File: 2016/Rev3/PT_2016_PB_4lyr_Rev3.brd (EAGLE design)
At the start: 155.7 x 202.7 mm, 168 parts, among them Q1 MOSFET-NCHANNELFDD8780, Q12 2N7002, Q2 MMBT2222A, Q3 MOSFET-NCHANNELFDD8780, Q4 MMBT2222A

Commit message: Final Power Board 2016 Rev 2
generated gerbers
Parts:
- moved C4 0.25 mm to (63.5, 78.7)
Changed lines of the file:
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@@
 <setting verticaltext="up"/>
 </settings>
-<grid distance="0.005" unitdist="inch" unit="inch" style="lines" multiple="1" display="yes" altdistance="0.005" altunitdist="inch" altunit="inch"/>
+<grid distance="0.01" unitdist="inch" unit="inch" style="lines" multiple="1" display="yes" altdistance="0.005" altunitdist="inch" altunit="inch"/>
 <layers>
 <layer number="1" name="Top" color="4" fill="1" visible="yes" active="yes"/>
@@
 <layer number="17" name="Pads" color="11" fill="1" visible="yes" active="yes"/>
 <layer number="18" name="Vias" color="11" fill="1" visible="yes" active="yes"/>
-<layer number="19" name="Unrouted" color="6" fill="1" visible="yes" active="yes"/>
+<layer number="19" name="Unrouted" color="6" fill="1" visible="no" active="yes"/>
 <layer number="20" name="Dimension" color="13" fill="1" visible="yes" active="yes"/>
 <layer number="21" name="tPlace" color="7" fill="1" visible="yes" active="yes"/>
-<layer number="22" name="bPlace" color="7" fill="1" visible="yes" active="yes"/>
-<layer number="23" name="tOrigins" color="15" fill="1" visible="yes" active="yes"/>
-<layer number="24" name="bOrigins" color="15" fill="1" visible="yes" active="yes"/>
+<layer number="22" name="bPlace" color="7" fill="1" visible="no" active="yes"/>
+<layer number="23" name="tOrigins" color="15" fill="1" visible="no" active="yes"/>
+<layer number="24" name="bOrigins" color="15" fill="1" visible="no" active="yes"/>
 <layer number="25" name="tNames" color="7" fill="1" visible="no" active="yes"/>
 <layer number="26" name="bNames" color="7" fill="1" visible="no" active="yes"/>
@@
 <layer number="37" name="tTest" color="7" fill="1" visible="no" active="yes"/>
 <layer number="38" name="bTest" color="7" fill="1" visible="no" active="yes"/>
-<layer number="39" name="tKeepout" color="4" fill="11" visible="yes" active="yes"/>
+<layer number="39" name="tKeepout" color="4" fill="11" visible="no" active="yes"/>
 <layer number="40" name="bKeepout" color="1" fill="11" visible="no" active="yes"/>
-<layer number="41" name="tRestrict" color="4" fill="10" visible="yes" active="yes"/>
-<layer number="42" name="bRestrict" color="1" fill="10" visible="yes" active="yes"/>
+<layer number="41" name="tRestrict" color="4" fill="10" visible="no" active="yes"/>
+<layer number="42" name="bRestrict" color="1" fill="10" visible="no" active="yes"/>
 <layer number="43" name="vRestrict" color="2" fill="10" visible="no" active="yes"/>
 <layer number="44" name="Drills" color="7" fill="1" visible="no" active="yes"/>
-<layer number="45" name="Holes" color="7" fill="1" visible="no" active="yes"/>
+<layer number="45" name="Holes" color="7" fill="1" visible="yes" active="yes"/>
 <layer number="46" name="Milling" color="3" fill="1" visible="no" active="yes"/>
 <layer number="47" name="Measures" color="7" fill="1" visible="no" active="yes"/>
@@
 <layer number="49" name="Reference" color="7" fill="1" visible="yes" active="yes"/>
 <layer number="50" name="dxf" color="7" fill="1" visible="no" active="yes"/>
-<layer number="51" name="tDocu" color="7" fill="1" visible="yes" active="yes"/>
-<layer number="52" name="bDocu" color="7" fill="1" visible="yes" active="yes"/>
+<layer number="51" name="tDocu" color="7" fill="1" visible="no" active="yes"/>
+<layer number="52" name="bDocu" color="7" fill="1" visible="no" active="yes"/>
 <layer number="91" name="Nets" color="2" fill="1" visible="no" active="no"/>
 <layer number="92" name="Busses" color="1" fill="1" visible="no" active="no"/>
@@
 <text x="25.4" y="162.814" size="1.778" layer="21" font="vector" ratio="15" rot="SR270">+5V</text>
 <text x="25.4" y="148.59" size="1.778" layer="21" font="vector" ratio="15" rot="SR270">+12V</text>
-<text x="49.276" y="13.97" size="2.54" layer="21" ratio="15" rot="SR270">M1</text>
-<text x="49.53" y="29.718" size="2.54" layer="21" ratio="15" rot="SR270">M2</text>
-<text x="49.276" y="45.212" size="2.54" layer="21" ratio="15" rot="SR270">M3</text>
-<text x="49.276" y="61.214" size="2.54" layer="21" ratio="15" rot="SR270">M4</text>
-<text x="49.276" y="76.962" size="2.54" layer="21" ratio="15" rot="SR270">M5</text>
-<text x="49.276" y="92.456" size="2.54" layer="21" ratio="15" rot="SR270">M6</text>
-<text x="49.276" y="108.458" size="2.54" layer="21" ratio="15" rot="SR270">A1</text>
-<text x="49.276" y="124.206" size="2.54" layer="21" ratio="15" rot="SR270">A2</text>
-<text x="135.636" y="104.013" size="2.54" layer="21" font="vector" ratio="15" rot="R270">RS-485</text>
+<text x="49.276" y="13.97" size="2.54" layer="21" font="vector" ratio="15" rot="SR270">M1</text>
+<text x="49.53" y="29.718" size="2.54" layer="21" font="vector" ratio="15" rot="SR270">M2</text>
+<text x="49.276" y="45.212" size="2.54" layer="21" font="vector" ratio="15" rot="SR270">M3</text>
+<text x="49.276" y="61.214" size="2.54" layer="21" font="vector" ratio="15" rot="SR270">M4</text>
+<text x="49.276" y="76.962" size="2.54" layer="21" font="vector" ratio="15" rot="SR270">M5</text>
+<text x="49.276" y="92.456" size="2.54" layer="21" font="vector" ratio="15" rot="SR270">M6</text>
+<text x="49.276" y="108.458" size="2.54" layer="21" font="vector" ratio="15" rot="SR270">A1</text>
+<text x="49.276" y="124.206" size="2.54" layer="21" font="vector" ratio="15" rot="SR270">A2</text>
+<text x="135.636" y="104.013" size="2.54" layer="21" font="vector" ratio="10" rot="R270">RS-485</text>
 <text x="141.097" y="26.162" size="2.54" layer="21" font="vector" ratio="15" rot="SR270">+ -</text>
 <hole x="112.014" y="196.596" drill="3.199890625"/>
@@
 <param name="mtCopper" value="0.035559375mm 0.035559375mm 0.035559375mm 0.035559375mm 0.035559375mm 0.035559375mm 0.035559375mm 0.035559375mm 0.035559375mm 0.035559375mm 0.035559375mm 0.035559375mm 0.035559375mm 0.035559375mm 0.035559375mm 0.035559375mm"/>
 <param name="mtIsolate" value="1.501140625mm 0.149859375mm 0.200659375mm 0.149859375mm 0.200659375mm 0.149859375mm 0.200659375mm 0.149859375mm 0.200659375mm 0.149859375mm 0.200659375mm 0.149859375mm 0.200659375mm 0.149859375mm 0.200659375mm"/>
-<param name="mdWireWire" value="8mil"/>
-<param name="mdWirePad" value="8mil"/>
-<param name="mdWireVia" value="8mil"/>
-<param name="mdPadPad" value="8mil"/>
-<param name="mdPadVia" value="8mil"/>
-<param name="mdViaVia" value="8mil"/>
-<param name="mdSmdPad" value="8mil"/>
-<param name="mdSmdVia" value="8mil"/>
-<param name="mdSmdSmd" value="8mil"/>
+<param name="mdWireWire" value="5mil"/>
+<param name="mdWirePad" value="5mil"/>
+<param name="mdWireVia" value="5mil"/>
+<param name="mdPadPad" value="5mil"/>
+<param name="mdPadVia" value="5mil"/>
+<param name="mdViaVia" value="5mil"/>
+<param name="mdSmdPad" value="5mil"/>
+<param name="mdSmdVia" value="5mil"/>
+<param name="mdSmdSmd" value="5mil"/>
 <param name="mdViaViaSameLayer" value="8mil"/>
 <param name="mnLayersViaInSmd" value="2"/>
@@
 <element name="C2" library="MRDT-2014-All" package="C_12.5MM" value="1mF" x="63.5" y="51.308"/>
 <element name="C3" library="MRDT-2014-All" package="C_12.5MM" value="1mF" x="63.5" y="37.592"/>
-<element name="C4" library="MRDT-2014-All" package="C_12.5MM" value="1mF" x="63.5" y="78.486"/>
+<element name="C4" library="MRDT-2014-All" package="C_12.5MM" value="1mF" x="63.5" y="78.74"/>
 <element name="R3" library="resistor" package="R1206" value="100k 1%" x="85.598" y="136.652" rot="R270"/>
 <element name="R4" library="resistor" package="R1206" value="10kΩ 1%" x="88.138" y="136.652" rot="R90"/>
@@
 <wire x1="132.458" y1="146.05" x2="130.556" y2="146.05" width="0.3048" layer="1"/>
 <via x="130.556" y="146.05" extent="1-16" drill="0.381"/>
-<wire x1="130.556" y1="146.05" x2="115.697" y2="131.191" width="0.3048" layer="16"/>
-<wire x1="115.697" y1="131.191" x2="99.822" y2="131.191" width="0.3048" layer="16"/>
+<wire x1="130.556" y1="146.05" x2="115.697" y2="131.191" width="0.3048" layer="2"/>
+<wire x1="115.697" y1="131.191" x2="99.822" y2="131.191" width="0.3048" layer="2"/>
 </signal>
 <signal name="N$4">
@@
 <wire x1="153.519" y1="17.689" x2="146.431" y2="24.777" width="0.3048" layer="1"/>
 <wire x1="146.431" y1="24.777" x2="154.432" y2="32.778" width="0.762" layer="2"/>
-<wire x1="154.432" y1="32.778" x2="154.432" y2="188.214" width="0.762" layer="2"/>
-<wire x1="154.432" y1="188.214" x2="154.432" y2="194.818" width="0.762" layer="2"/>
+<wire x1="154.432" y1="32.778" x2="154.432" y2="188.976" width="0.762" layer="2"/>
+<wire x1="154.432" y1="188.976" x2="154.432" y2="194.818" width="0.762" layer="2"/>
 <wire x1="154.432" y1="194.818" x2="152.654" y2="196.596" width="0.762" layer="2"/>
-<wire x1="89.154" y1="196.596" x2="97.536" y2="188.214" width="0.762" layer="2"/>
-<wire x1="97.536" y1="188.214" x2="154.432" y2="188.214" width="0.762" layer="2"/>
-<wire x1="97.536" y1="188.214" x2="97.536" y2="121.92" width="0.762" layer="2"/>
-<wire x1="97.536" y1="121.92" x2="94.488" y2="118.872" width="0.762" layer="2"/>
+<wire x1="89.154" y1="196.596" x2="96.774" y2="188.976" width="0.762" layer="2"/>
+<wire x1="96.774" y1="188.976" x2="154.432" y2="188.976" width="0.762" layer="2"/>
+<wire x1="96.774" y1="188.976" x2="96.774" y2="121.158" width="0.762" layer="2"/>
+<wire x1="96.774" y1="121.158" x2="94.488" y2="118.872" width="0.762" layer="2"/>
 <wire x1="94.488" y1="118.872" x2="86.106" y2="118.872" width="0.762" layer="2"/>
 </signal>
@@
 <wire x1="139.446" y1="144.188" x2="139.446" y2="143.002" width="0.3048" layer="1"/>
 <via x="139.446" y="143.002" extent="1-16" drill="0.381"/>
-<wire x1="139.446" y1="143.002" x2="120.015" y2="123.571" width="0.3048" layer="16"/>
-<wire x1="120.015" y1="123.571" x2="99.822" y2="123.571" width="0.3048" layer="16"/>
+<wire x1="139.446" y1="143.002" x2="120.015" y2="123.571" width="0.3048" layer="2"/>
+<wire x1="120.015" y1="123.571" x2="99.822" y2="123.571" width="0.3048" layer="2"/>
 </signal>
 <signal name="N$14">

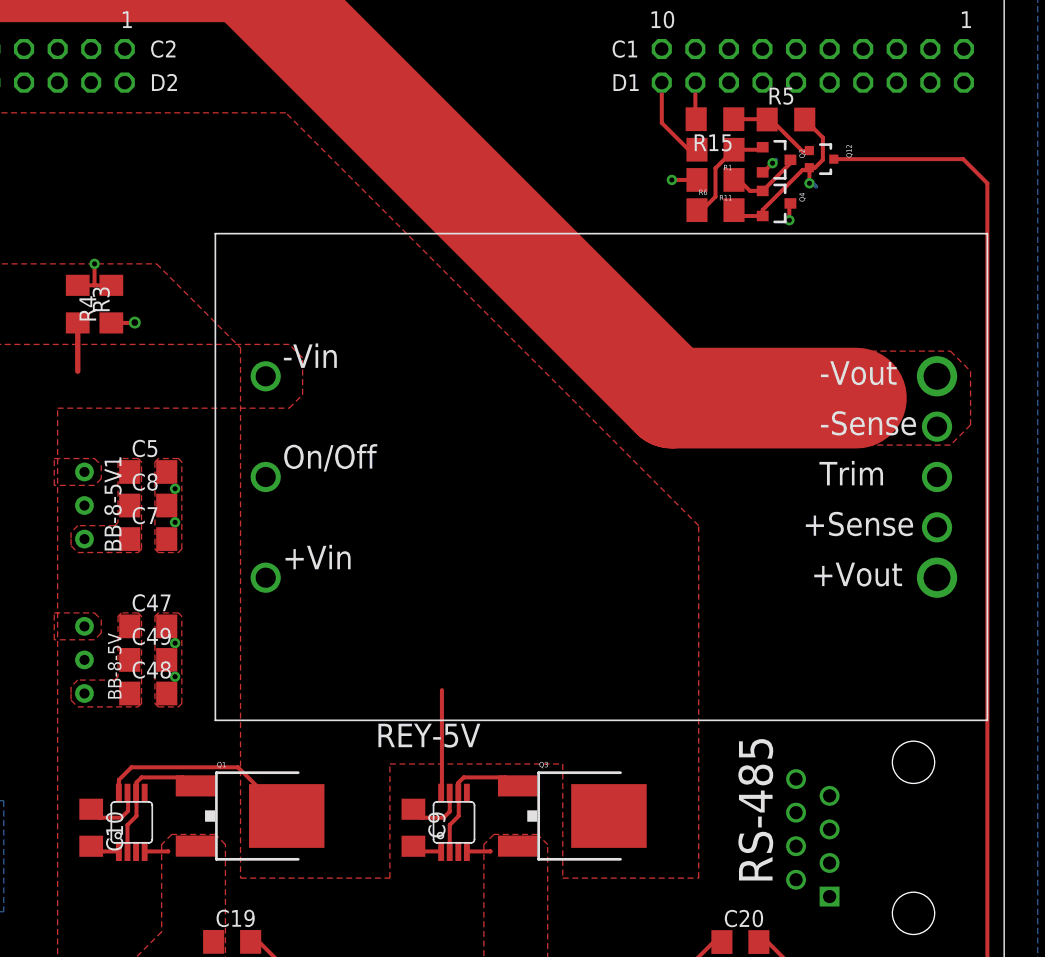
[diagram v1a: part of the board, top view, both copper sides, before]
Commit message: Swapped LM74670 with LM5050
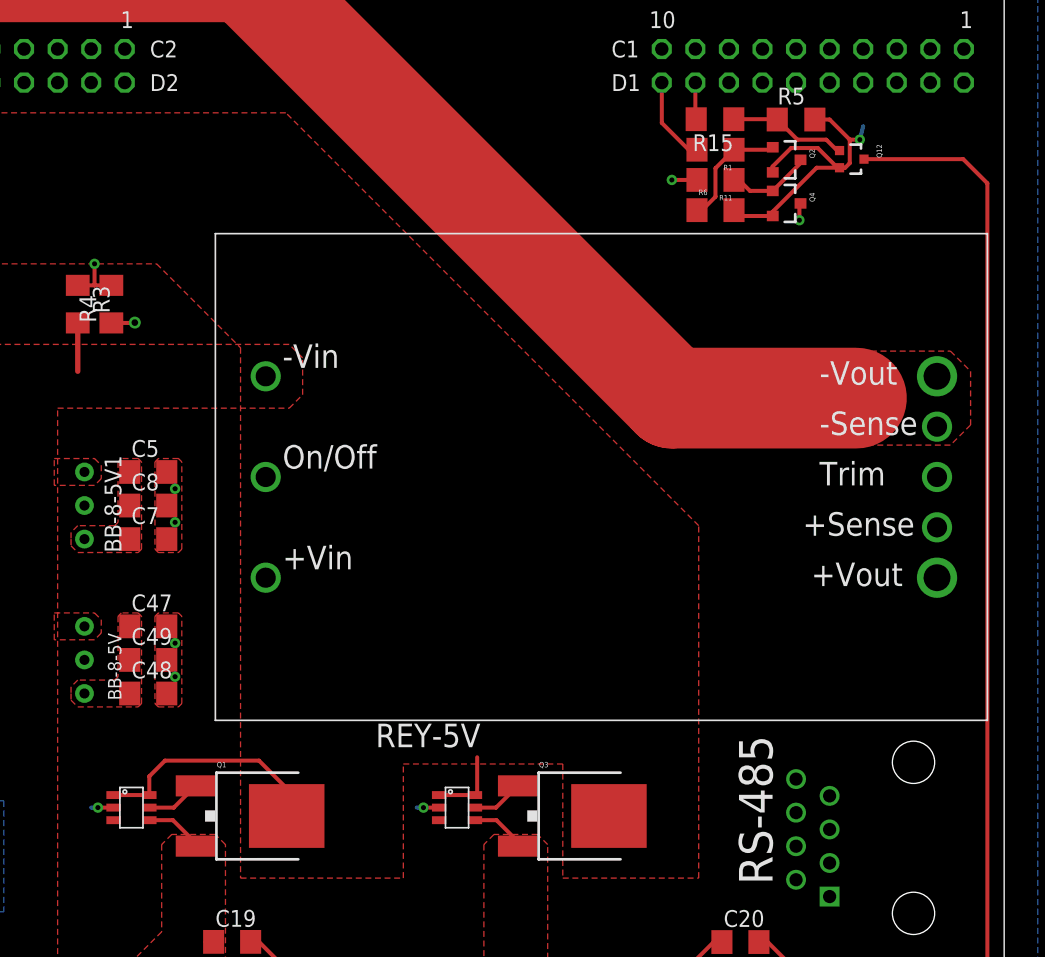
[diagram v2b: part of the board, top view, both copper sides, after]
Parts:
- removed C10, C9: 1uF, resistor:C1206
- removed U$13: LM74670-Q1, LM74670-Q1:LM74670-Q1
- added U$6: LM5050, LM5050:LM5050
- U$9: value LM74670-Q1 -> LM5050; device LM74670-Q1:LM74670-Q1 -> LM5050:LM5050
- moved U$9 24.4 mm to (89.7, 98.6), turned to 270 degrees
- moved Q12 2.29 mm to (144.2, 147.6)
- moved Q2 0.76 mm to (139.2, 147.6)
- moved Q4 0.76 mm to (139.2, 144.3)
- moved R5 0.76 mm to (140.0, 150.6)
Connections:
- removed net N$10: C10.2, U$13.P$5
- removed net N$7: C9.1, U$9.P$2
- removed net N$8: C9.2, U$9.P$5
- removed net N$9: C10.1, U$13.P$2
- net GND: now also U$6.P$1, U$9.P$1
- net N$1: now also U$6.P$6; no longer U$9.P$8
- net N$2: now also U$9.P$6; no longer U$13.P$8
- net N$3: now also U$6.P$2; no longer U$9.P$3, U$9.P$6
- net N$33: now also U$6.P$4, U$6.P$5, U$9.P$4, U$9.P$5; no longer U$13.P$1, U$9.P$1
- net N$5: now also U$9.P$2; no longer U$13.P$3, U$13.P$6
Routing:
- net GND: track 201.1 -> 213.0 mm, vias 49 -> 50
- net N$3: track 10.4 -> 3.93 mm
- net N$5: track 10.4 -> 4.18 mm
- net N$9: track 4.63 -> 0.00 mm
- net N$7: track 4.59 -> 0.00 mm
- net N$2: track 2.43 -> 5.05 mm
- net N$1: track 10.3 -> 12.8 mm
- net N$4: track 187.3 -> 185.0 mm
- net N$8: track 2.26 -> 0.00 mm
- net N$10: track 2.26 -> 0.00 mm
- net N$114: track 6.75 -> 8.99 mm
- net N$15: track 5.74 -> 6.50 mm
- net N$14: track 8.21 -> 8.97 mm
- net N$11: track 49.0 -> 49.7 mm

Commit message: Fixed some routing
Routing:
- net GND: track 213.0 -> 209.0 mm, vias 50 -> 51
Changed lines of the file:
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@@
 <contactref element="R6" pad="2"/>
 <wire x1="135.258" y1="143.764" x2="135.7" y2="143.322" width="0.3048" layer="1"/>
-<wire x1="135.7" y1="143.322" x2="138.192" y2="143.322" width="0.3048" layer="1"/>
 <wire x1="47.498" y1="150.746" x2="47.498" y2="150.876" width="0.3048" layer="1"/>
 <wire x1="47.498" y1="150.876" x2="47.752" y2="151.13" width="0.3048" layer="1"/>
@@
 <wire x1="143.6728" y1="146.9748" x2="143.2454" y2="146.9748" width="0.3048" layer="1"/>
 <wire x1="138.192" y1="143.322" x2="138.176" y2="143.338" width="0.3048" layer="1"/>
-<wire x1="138.176" y1="143.338" x2="138.176" y2="143.637" width="0.3048" layer="1"/>
-<wire x1="138.176" y1="143.637" x2="141.5138" y2="146.9748" width="0.3048" layer="1"/>
-<wire x1="141.5138" y1="146.9748" x2="143.0932" y2="146.9748" width="0.3048" layer="1"/>
 <wire x1="138.192" y1="146.624" x2="138.176" y2="146.64" width="0.3048" layer="1"/>
 <wire x1="138.176" y1="146.64" x2="138.176" y2="147.066" width="0.3048" layer="1"/>
@@
 <via x="144.78" y="149.098" extent="1-16" drill="0.381"/>
 <wire x1="144.78" y1="149.098" x2="145.034" y2="150.114" width="0.3048" layer="16"/>
+<wire x1="138.192" y1="143.322" x2="135.7" y2="143.322" width="0.3048" layer="1"/>
+<wire x1="138.192" y1="143.322" x2="136.906" y2="143.322" width="0.3048" layer="1"/>
+<wire x1="136.906" y1="143.322" x2="136.906" y2="142.494" width="0.3048" layer="1"/>
+<via x="136.906" y="142.494" extent="1-16" drill="0.381"/>
+<wire x1="136.906" y1="142.494" x2="136.906" y2="141.986" width="0.3048" layer="16"/>
 </signal>
 <signal name="V_BATT">
